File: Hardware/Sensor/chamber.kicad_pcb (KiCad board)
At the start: 2 copper layers, 83 x 95 mm, 57 parts, among them J1 Conn_01x15_Female, J2 Conn_01x15_Female, J3 RF_Shield_One_Piece, J4 Conn_Coaxial, J5 Conn_01x03_Male, J6 Conn_01x03_Male, J7 Conn_01x04_Female, Q1 Q_PMOS_GDS, Q2 Q_PMOS_GDS, Q3 Q_NMOS_GDS, Q4 Q_NMOS_GDS, U1 Nucleo32, U2 MCP3425A0T-ECH, U3 LMC662, U4 LM358

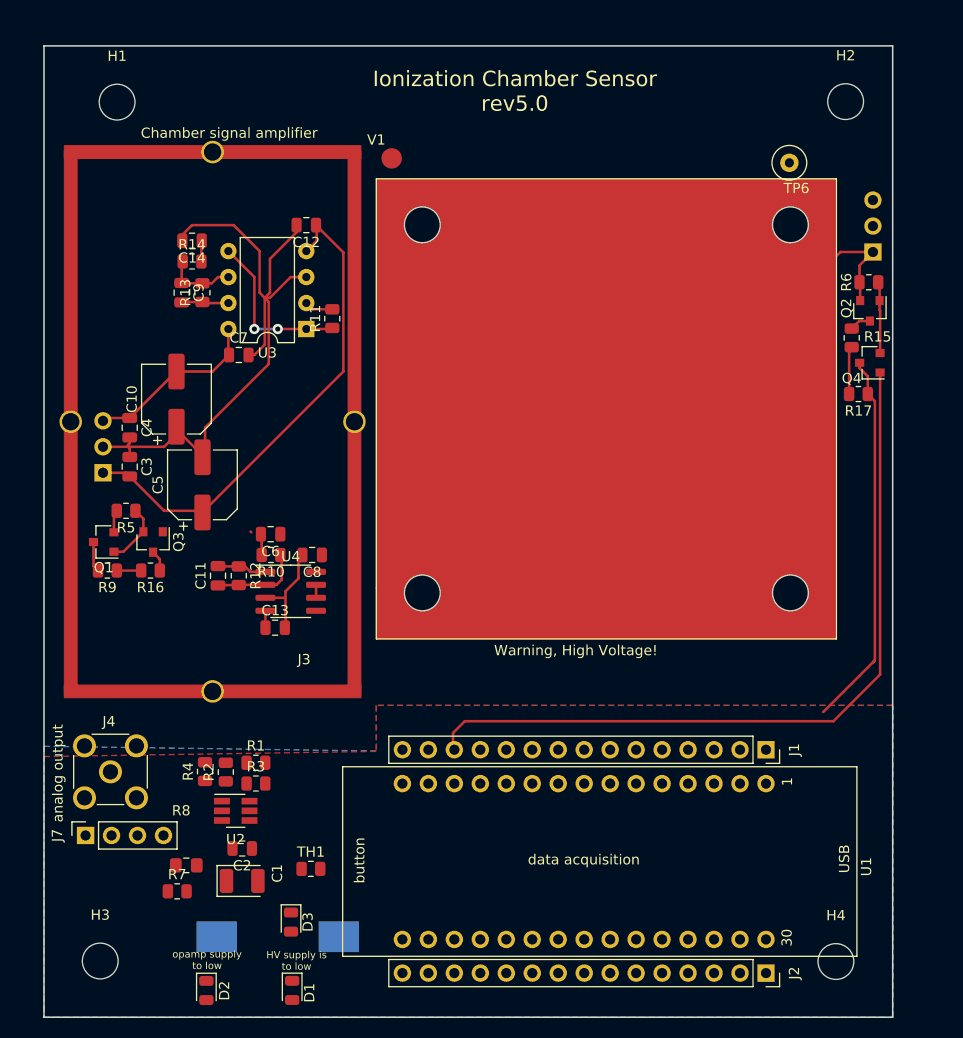
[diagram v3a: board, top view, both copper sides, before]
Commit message: switched from stm32 nucleo to stm8, added user interface, added draft of pcb routing
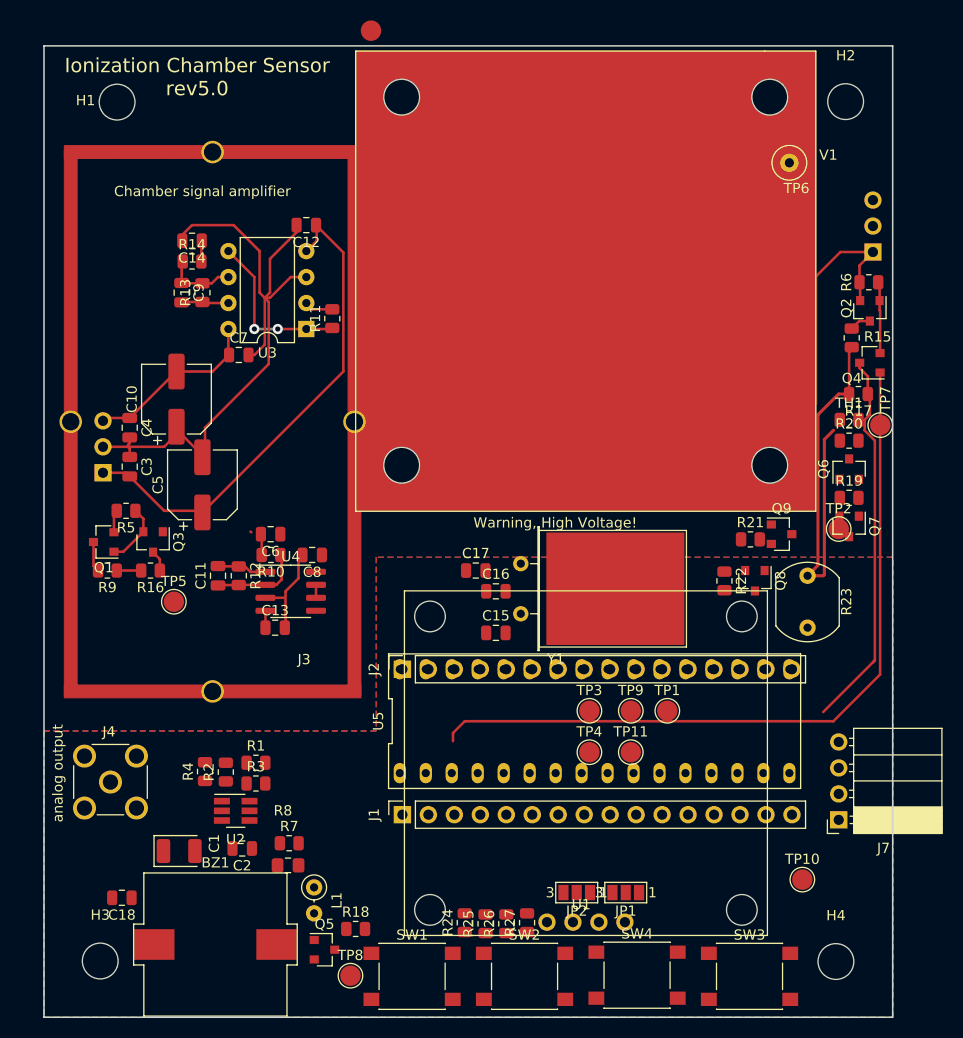
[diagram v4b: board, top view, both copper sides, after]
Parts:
- removed D1, D2, D3: red, LED_SMD:LED_0805_2012Metric
- added C15: 470n, Capacitor_SMD:C_0805_2012Metric, F.Cu at (101.2, 81.4)
- added C16: 22p, Capacitor_SMD:C_0805_2012Metric, F.Cu at (101.2, 77.3)
- added C17: 22p, Capacitor_SMD:C_0805_2012Metric, F.Cu at (99.2, 75.3)
- added C18: 100n, Capacitor_SMD:C_0805_2012Metric, F.Cu at (64.6, 107.3)
- added JP1: SolderJumper_3_Open, Jumper:SolderJumper-3_P1.3mm_Open_Pad1.0x1.5mm_NumberLabels, F.Cu at (113.9, 106.8)
- added JP2: SolderJumper_3_Open, Jumper:SolderJumper-3_P1.3mm_Open_Pad1.0x1.5mm_NumberLabels, F.Cu at (109.1, 106.8)
- added L1: L, Inductor_THT:L_Axial_L5.3mm_D2.2mm_P2.54mm_Vertical_Vishay_IM-1, F.Cu at (83.4, 106.3)
- added Q5: Q_NPN_BEC, Package_TO_SOT_SMD:SOT-23, F.Cu at (84.4, 112.4)
- added Q6: Q_PMOS_GDS, Package_TO_SOT_SMD:SOT-23, F.Cu at (135.7, 65.4)
- added Q7: Q_NMOS_GDS, Package_TO_SOT_SMD:SOT-23, F.Cu at (135.7, 71.0)
- added Q8: Q_PMOS_GDS, Package_TO_SOT_SMD:SOT-23, F.Cu at (126.5, 76.3)
- added Q9: Q_NMOS_GDS, Package_TO_SOT_SMD:SOT-23, F.Cu at (129.1, 71.8)
- added R18: 10k, Resistor_SMD:R_0805_2012Metric, F.Cu at (87.5, 110.4)
- added R19: TBD, Resistor_SMD:R_0805_2012Metric, F.Cu at (135.7, 68.2)
- added R20: TBD, Resistor_SMD:R_0805_2012Metric, F.Cu at (135.7, 62.6)
- added R21: TBD, Resistor_SMD:R_0805_2012Metric, F.Cu at (126.1, 72.3)
- added R22: TBD, Resistor_SMD:R_0805_2012Metric, F.Cu at (123.5, 76.3)
- added R23: R_PHOTO, OptoDevice:R_LDR_7x6mm_P5.1mm_Vertical, F.Cu at (131.7, 75.8)
- added R24: TBD, Resistor_SMD:R_0805_2012Metric, F.Cu at (98.1, 109.8)
- added R25: TBD, Resistor_SMD:R_0805_2012Metric, F.Cu at (100.2, 109.9)
- added R26: TBD, Resistor_SMD:R_0805_2012Metric, F.Cu at (102.2, 109.9)
- added R27: TBD, Resistor_SMD:R_0805_2012Metric, F.Cu at (104.2, 109.8)
- added SW1: UP, Button_Switch_SMD:SW_SPST_PTS645, F.Cu at (93.0, 115.0)
- added SW2: DOWN, Button_Switch_SMD:SW_SPST_PTS645, F.Cu at (104.0, 115.0)
- added SW3: LEFT, Button_Switch_SMD:SW_SPST_PTS645, F.Cu at (126.0, 115.0)
- added SW4: RIGHT, Button_Switch_SMD:SW_SPST_PTS645, F.Cu at (115.0, 114.9)
- added TP1: TestPoint, TestPoint:TestPoint_Pad_D2.0mm, F.Cu at (118.0, 89.0)
- added TP10: TestPoint, TestPoint:TestPoint_Pad_D2.0mm, F.Cu at (131.2, 105.5)
- added TP11: TestPoint, TestPoint:TestPoint_Pad_D2.0mm, F.Cu at (114.4, 93.1)
- added TP2: TestPoint, TestPoint:TestPoint_Pad_D2.0mm, F.Cu at (134.7, 71.2)
- added TP3: TestPoint, TestPoint:TestPoint_Pad_D2.0mm, F.Cu at (110.3, 89.0)
- added TP4: TestPoint, TestPoint:TestPoint_Pad_D2.0mm, F.Cu at (110.3, 93.1)
- added TP5: TestPoint, TestPoint:TestPoint_Pad_D2.0mm, F.Cu at (69.7, 78.4)
- added TP7: TestPoint, TestPoint:TestPoint_Pad_D2.0mm, F.Cu at (138.8, 61.1)
- added TP8: TestPoint, TestPoint:TestPoint_Pad_D2.0mm, F.Cu at (87.0, 114.9)
- added TP9: TestPoint, TestPoint:TestPoint_Pad_D2.0mm, F.Cu at (114.4, 89.0)
- added U5: STM8S105K4B6, IonizationChamber:DIP-32_400_ELL, F.Cu at (110.8, 90.0)
- added Y1: Crystal, Crystal:Crystal_HC18-U_Horizontal_1EP_style1, F.Cu at (103.6, 79.5)
- BZ1: moved to F.Cu
- J1, J2: value Conn_01x15_Female -> Conn_01x16_Female; footprint Connector_PinSocket_2.54mm:PinSocket_1x15_P2.54mm_Vertical -> Connector_PinSocket_2.54mm:PinSocket_1x16_P2.54mm_Vertical
- J7: value Conn_01x04_Female -> UART; footprint Connector_PinSocket_2.54mm:PinSocket_1x04_P2.54mm_Vertical -> Connector_PinSocket_2.54mm:PinSocket_1x04_P2.54mm_Horizontal
- R7, R8: value 2k2 -> 4k7
- U1: value Nucleo32 -> SSD1306; footprint IonizationChamber:Nucleo32 -> IonizationChamber:SSD1306
- moved J7 73.7 mm to (134.7, 99.7), turned to 180 degrees
- moved TH1 68.5 mm to (135.7, 60.6)
- moved J2 46.3 mm to (92.1, 85.0), turned to 90 degrees
- moved J1 36.1 mm to (92.1, 99.2), turned to 90 degrees
- moved U1 31.2 mm to (110.0, 111.0), turned to 180 degrees
- moved V1 12.7 mm to (87.5, 24.5)
- moved R7 11.9 mm to (81.0, 102.0)
- moved R8 9.95 mm to (80.9, 104.1)
- moved C1 6.82 mm to (70.2, 102.7)
- moved BZ1 6.14 mm to (73.8, 111.9)
- moved J4 1.00 mm to (63.5, 96.0)
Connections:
- BZ1 pad 1: (no net) -> +5V
- BZ1 pad 2: (no net) -> Net-(BZ1-Pad2)
- J1 pad 1: Net-(J1-Pad1) -> BATTERY_MEASSURE_VALUE
- J1 pad 10: BATTERY_MEASSURE_ENA -> /DataAcquisition/STM8_1_10
- J1 pad 11: BATTERY_MEASSURE_VALUE -> /DataAcquisition/STM8_1_11
- J1 pad 12: CHAMBER_VOLTAGE_MEASSURE_VALUE -> /DataAcquisition/STM8_1_12
- J1 pad 13: CHAMBER_VOLTAGE_MEASSURE_ENA -> /DataAcquisition/STM8_1_13
- J1 pad 14: Net-(J1-Pad14) -> /DataAcquisition/STM8_1_14
- J1 pad 15: Net-(J1-Pad15) -> /DataAcquisition/STM8_1_15
- J1 pad 2: Net-(J1-Pad2) -> /DataAcquisition/STM8_1_2
- J1 pad 3: Net-(J1-Pad3) -> /DataAcquisition/STM8_1_3
- J1 pad 4: Net-(J1-Pad4) -> /DataAcquisition/STM8_1_4
- J1 pad 5: Net-(J1-Pad5) -> /DataAcquisition/STM8_1_5
- J1 pad 6: Net-(J1-Pad6) -> /DataAcquisition/STM8_1_6
- J1 pad 7: Net-(J1-Pad7) -> /DataAcquisition/STM8_1_7
- J1 pad 8: Net-(J1-Pad8) -> /DataAcquisition/STM8_1_8
- J1 pad 9: Net-(J1-Pad9) -> /DataAcquisition/STM8_1_9
- J2 pad 1: Net-(J2-Pad1) -> /DataAcquisition/STM8_1_32
- J2 pad 10: Net-(J2-Pad10) -> /DataAcquisition/STM8_1_23
- J2 pad 11: Net-(J2-Pad11) -> /DataAcquisition/STM8_1_22
- J2 pad 12: Net-(J2-Pad12) -> /DataAcquisition/STM8_1_21
- J2 pad 13: Net-(J2-Pad13) -> /DataAcquisition/STM8_1_20
- J2 pad 14: Net-(J2-Pad14) -> /DataAcquisition/STM8_1_19
- J2 pad 15: Net-(J2-Pad15) -> /DataAcquisition/STM8_1_18
- J2 pad 2: Net-(J2-Pad2) -> /DataAcquisition/STM8_1_31
- J2 pad 3: Net-(J2-Pad3) -> /DataAcquisition/STM8_1_30
- J2 pad 4: Net-(J2-Pad4) -> /DataAcquisition/STM8_1_29
- J2 pad 5: Net-(J2-Pad5) -> /DataAcquisition/STM8_1_28
- J2 pad 6: Net-(J2-Pad6) -> /DataAcquisition/STM8_1_27
- J2 pad 7: Net-(J2-Pad7) -> /DataAcquisition/STM8_1_26
- J2 pad 8: Net-(J2-Pad8) -> /DataAcquisition/STM8_1_25
- J2 pad 9: Net-(J2-Pad9) -> /DataAcquisition/STM8_1_24
- R15 pad 1: CHAMBER_VOLTAGE_MEASSURE_VALUE -> BATTERY_MEASSURE_VALUE
- R17 pad 2: CHAMBER_VOLTAGE_MEASSURE_VALUE -> BATTERY_MEASSURE_VALUE
- R7 pad 1: /DataAcquisition/SCL -> SCL
- R8 pad 1: /DataAcquisition/SDA -> SDA
- TH1 pad 1: (no net) -> BATTERY_MEASSURE_VALUE
- U1 pad 1: Net-(J1-Pad1) -> Net-(JP2-Pad2)
- U1 pad 2: Net-(J1-Pad2) -> Net-(JP1-Pad2)
- U1 pad 3: Net-(J1-Pad3) -> SCL
- U1 pad 4: Net-(J1-Pad4) -> SDA
- U2 pad 3: /DataAcquisition/SCL -> SCL
- U2 pad 4: /DataAcquisition/SDA -> SDA
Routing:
- net BATTERY_MEASSURE_VALUE: track 2.39 -> 43.8 mm
- net CHAMBER_VOLTAGE_MEASSURE_VALUE: track 5.18 -> 0.00 mm
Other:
- board text removed: "HV supply is to low"
- board text removed: "data acquisition"
- board text removed: "opamp supply to low"

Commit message: finished pcb design
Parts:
- removed TP11, TP3, TP4, TP9: TestPoint, TestPoint:TestPoint_Pad_D2.0mm
- added C19: 100n, Capacitor_SMD:C_0805_2012Metric, F.Cu at (100.9, 87.6)
- added C20: 100n, Capacitor_SMD:C_0805_2012Metric, F.Cu at (97.6, 87.6)
- added C21: TBD, Capacitor_SMD:C_0805_2012Metric, F.Cu at (130.1, 80.6)
- added C22: 470n, Capacitor_SMD:C_0805_2012Metric, F.Cu at (105.8, 86.2)
- added C23: 470n, Capacitor_SMD:C_0805_2012Metric, F.Cu at (105.8, 88.3)
- added C24: 100n, Capacitor_SMD:C_0805_2012Metric, F.Cu at (122.3, 87.5)
- added C25: 4u7, Capacitor_Tantalum_SMD:CP_EIA-3528-21_Kemet-B, F.Cu at (136.5, 106.8)
- added C26: 100n, Capacitor_SMD:C_0805_2012Metric, F.Cu at (133.7, 106.6)
- added C27: 100n, Capacitor_SMD:C_0805_2012Metric, F.Cu at (82.1, 107.1)
- added J8: USB_B_Micro, Connector_USB:USB_Micro-B_Molex-105017-0001, F.Cu at (137.0, 99.2)
- added J9: Conn_01x04, Connector_PinSocket_2.54mm:PinSocket_1x04_P2.54mm_Vertical, F.Cu at (81.4, 103.0)
- added JP3: Jumper_2_Open, Jumper:SolderJumper-2_P1.3mm_Open_Pad1.0x1.5mm, F.Cu at (135.2, 80.9)
- added JP4: Jumper_2_Open, Jumper:SolderJumper-2_P1.3mm_Open_Pad1.0x1.5mm, F.Cu at (78.5, 102.7)
- added R28: TBD, Resistor_SMD:R_0805_2012Metric, F.Cu at (130.0, 78.6)
- added R29: 100R, Resistor_SMD:R_0805_2012Metric, F.Cu at (89.0, 101.0)
- added R30: 100R, Resistor_SMD:R_0805_2012Metric, F.Cu at (88.8, 91.9)
- added TP12: TestPoint, TestPoint:TestPoint_Pad_D2.0mm, F.Cu at (135.5, 83.3)
- added TP13: TestPoint, TestPoint:TestPoint_Pad_D2.0mm, F.Cu at (135.5, 85.9)
- C15: value 470n -> 100n
- R8: footprint Resistor_SMD:R_0805_2012Metric_Pad1.15x1.40mm_HandSolder -> Resistor_SMD:R_0805_2012Metric
- Y1: footprint Crystal:Crystal_HC18-U_Horizontal_1EP_style1 -> Crystal:Crystal_SMD_5032-2Pin_5.0x3.2mm_HandSoldering
- moved R23 76.7 mm to (60.0, 103.3)
- moved R22 65.2 mm to (64.6, 104.2)
- moved Q8 64.5 mm to (67.7, 102.7), turned to 180 degrees
- moved Q9 63.5 mm to (73.8, 102.7)
- moved R21 63.2 mm to (70.7, 102.6), turned to 90 degrees
- moved TP10 62.3 mm to (69.2, 99.7)
- moved J2 42.7 mm to (130.2, 104.3), turned to 270 degrees
- moved J1 41.3 mm to (130.2, 83.2), turned to 270 degrees
- moved C16 21.6 mm to (120.2, 87.5), turned to 90 degrees
- moved R26 18.0 mm to (120.1, 108.1), turned to 180 degrees
- moved TP7 17.3 mm to (138.0, 78.4)
- moved TP1 17.1 mm to (129.1, 76.1)
- moved R27 15.9 mm to (120.1, 110.1), turned to 180 degrees
- moved C17 15.3 mm to (108.6, 87.4), turned to 90 degrees
- moved Y1 13.4 mm to (114.4, 87.5), turned to 180 degrees
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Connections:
- C15 pad 1: (no net) -> +5V
- J1 pad 1: BATTERY_MEASSURE_VALUE -> /DataAcquisition/STM8_1_1
- J1 pad 11: /DataAcquisition/STM8_1_11 -> +5V
- J1 pad 12: /DataAcquisition/STM8_1_12 -> +5V
- J1 pad 14: /DataAcquisition/STM8_1_14 -> +5V
- J1 pad 15: /DataAcquisition/STM8_1_15 -> GND
- J1 pad 16: SDA -> /DataAcquisition/STM8_1_16
- J1 pad 5: /DataAcquisition/STM8_1_5 -> (no net)
- J1 pad 6: /DataAcquisition/STM8_1_6 -> (no net)
- J1 pad 7: /DataAcquisition/STM8_1_7 -> (no net)
- J1 pad 8: /DataAcquisition/STM8_1_8 -> (no net)
- J1 pad 9: /DataAcquisition/STM8_1_9 -> GND
- J2 pad 13: /DataAcquisition/STM8_1_20 -> KEY_DOWN
- J2 pad 14: /DataAcquisition/STM8_1_19 -> KEY_UP
- J2 pad 15: /DataAcquisition/STM8_1_18 -> BUZZER
- J2 pad 16: SCL -> /DataAcquisition/STM8_1_17
- J2 pad 2: /DataAcquisition/STM8_1_31 -> KEY_LEFT
- J2 pad 3: /DataAcquisition/STM8_1_30 -> KEY_RIGHT
- J2 pad 6: /DataAcquisition/STM8_1_27 -> BATTERY_MEASSURE_ENA
- J2 pad 7: /DataAcquisition/STM8_1_26 -> CHAMBER_VOLTAGE_MEASSURE_ENA
- J2 pad 8: /DataAcquisition/STM8_1_25 -> R_PHOTO_VOLTAGE_MEASSURE_ENA
- J7 pad 1: (no net) -> GND
- J7 pad 2: (no net) -> /DataAcquisition/STM8_1_4
- J7 pad 3: (no net) -> /DataAcquisition/STM8_1_3
- J7 pad 4: (no net) -> Net-(J7-Pad4)
- Q7 pad 1: /DataAcquisition/THERMISTOR_VOLTAGE_MEASSURE_ENA -> /DataAcquisition/STM8_1_32
- R7 pad 1: SCL -> SDA
- R8 pad 1: SDA -> SCL
- TP1 pad 1: BATTERY_MEASSURE_VALUE -> /DataAcquisition/STM8_1_1
- TP2 pad 1: /DataAcquisition/THERMISTOR_VOLTAGE_MEASSURE_ENA -> /DataAcquisition/STM8_1_32
- U2 pad 1: Net-(R2-Pad1) -> Net-(R3-Pad1)
- U2 pad 6: Net-(R3-Pad1) -> Net-(R2-Pad1)
- U5 pad 1: BATTERY_MEASSURE_VALUE -> /DataAcquisition/STM8_1_1
- U5 pad 11: /DataAcquisition/STM8_1_11 -> +5V
- U5 pad 12: /DataAcquisition/STM8_1_12 -> +5V
- U5 pad 14: /DataAcquisition/STM8_1_14 -> +5V
- U5 pad 15: /DataAcquisition/STM8_1_15 -> GND
- U5 pad 16: SDA -> /DataAcquisition/STM8_1_16
- U5 pad 17: SCL -> /DataAcquisition/STM8_1_17
- U5 pad 18: /DataAcquisition/STM8_1_18 -> BUZZER
- U5 pad 19: /DataAcquisition/STM8_1_19 -> KEY_UP
- U5 pad 20: /DataAcquisition/STM8_1_20 -> KEY_DOWN
- U5 pad 25: /DataAcquisition/STM8_1_25 -> R_PHOTO_VOLTAGE_MEASSURE_ENA
- U5 pad 26: /DataAcquisition/STM8_1_26 -> CHAMBER_VOLTAGE_MEASSURE_ENA
- U5 pad 27: /DataAcquisition/STM8_1_27 -> BATTERY_MEASSURE_ENA
- U5 pad 30: /DataAcquisition/STM8_1_30 -> KEY_RIGHT
- U5 pad 31: /DataAcquisition/STM8_1_31 -> KEY_LEFT
- U5 pad 5: /DataAcquisition/STM8_1_5 -> (no net)
- U5 pad 9: /DataAcquisition/STM8_1_9 -> GND
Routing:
- net +5V: track 0.00 -> 268.7 mm, vias 0 -> 6
- net GND: track 116.5 -> 284.3 mm, vias 0 -> 91
- net BATTERY_MEASSURE_VALUE: track 43.8 -> 149.6 mm, vias 0 -> 5
- net KEY_LEFT: track 0.00 -> 74.2 mm, vias 0 -> 1
- net BATTERY_MEASSURE_ENA: track 0.00 -> 71.6 mm, vias 0 -> 4
- net SCL: track 0.00 -> 53.0 mm, vias 0 -> 2
- net R_PHOTO_VOLTAGE_MEASSURE_ENA: track 0.00 -> 52.3 mm, vias 0 -> 2
- net SDA: track 0.00 -> 52.2 mm, vias 0 -> 4
- net /DataAcquisition/STM8_1_6: track 0.00 -> 45.4 mm, vias 0 -> 1
- net analog_output: track 1.27 -> 43.7 mm
- net +BATT: track 19.8 -> 58.2 mm, vias 0 -> 2
- net /DataAcquisition/STM8_1_32: track 0.00 -> 37.6 mm, vias 0 -> 2
- net /DataAcquisition/STM8_1_4: track 0.00 -> 32.9 mm
- net /DataAcquisition/STM8_1_3: track 0.00 -> 30.7 mm
- net Net-(C6-Pad1): track 4.63 -> 29.3 mm, vias 0 -> 2
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
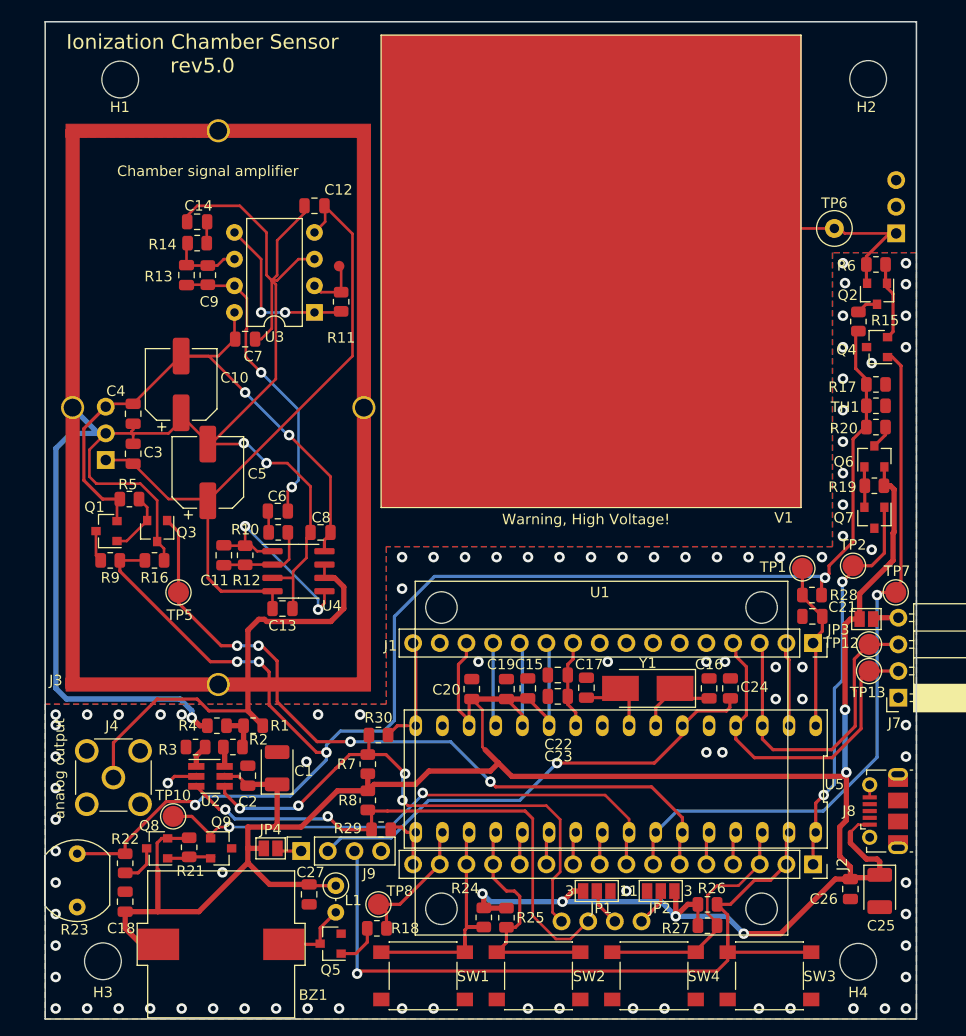
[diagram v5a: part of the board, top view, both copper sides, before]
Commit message: fix #249
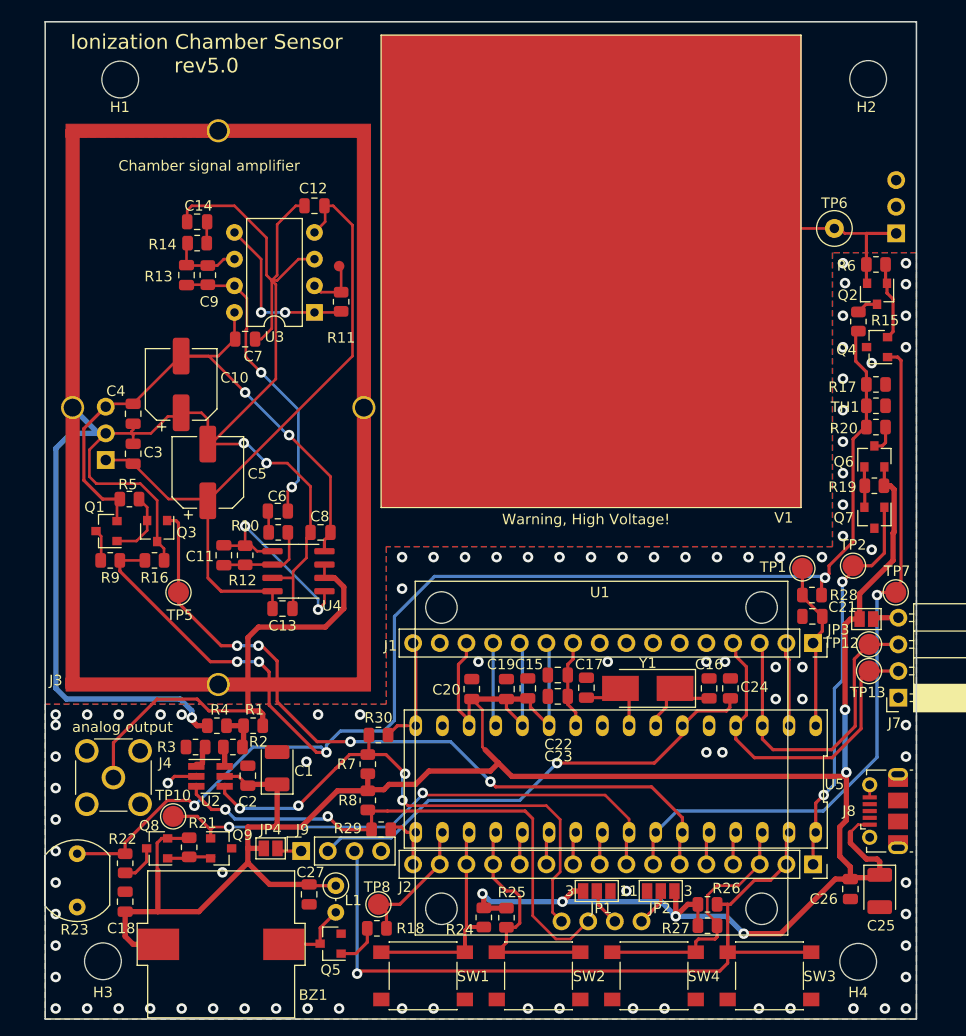
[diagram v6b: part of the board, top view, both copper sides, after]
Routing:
- net GND: track 284.3 -> 286.7 mm
- net /AnalogFrontend/CHAMBER_VOLTAGE: track 18.8 -> 20.1 mm
- net KEY_RIGHT: track 24.0 -> 24.9 mm
- net KEY_LEFT: track 74.2 -> 74.9 mm
- net Net-(Q1-Pad1): track 6.06 -> 6.60 mm
- net +5V: track 268.7 -> 269.2 mm
